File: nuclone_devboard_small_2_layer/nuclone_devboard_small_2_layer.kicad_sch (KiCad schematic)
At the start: 36 parts, among them J1 JTAG_2X05, J2 TYPE-C-31-M-12, J3 nuclone_small_left, J4 nuclone_small_right, SW1 RESET, SW2 Bootloader, U1 MCP1702-MB, U2 TPESD0504C6

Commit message: WIP redoing the template
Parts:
- removed C9: 100n, SquantorRcl:C_0805, symbol Device:C
- C1, C17, C2: footprint SquantorRcl:C_0603 -> SquantorCapacitor:C_0603
- C14, C4: footprint SquantorRcl:C_0402 -> SquantorCapacitor:C_0603
- F1: footprint SquantorRcl:F_0603_hand -> SquantorFuse:F_0603_hand
- FB1: footprint SquantorRcl:L_0603 -> SquantorInductor:L_0603
- H1, H2, H3, H4: footprint MountingHole:MountingHole_3.2mm_M3_Pad_Via -> SquantorPcbOutline:MountingHole_3.2mm_M3_Pad_Via
- R1, R13, R14, R2, R3, R4, R5, R6, R7, R8: footprint SquantorRcl:R_0402_hand -> SquantorResistor:R_0603_hand
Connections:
- net VSS: now also J2.S (Shield)

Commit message: WIP rerouting board and making it common with the medium board
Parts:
- added C5: 100n, SquantorCapacitor:C_0603, symbol Device:C
- added C6: 10u, SquantorCapacitor:C_0603, symbol Device:C
- added R9: 470, SquantorResistor:R_0603_hand, symbol Device:R
- R13: value 100 -> 470
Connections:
- net VBUS: now also C4.1, U2.5 (VDD), C6.1
- net VSS: now also C5.2, C6.2
- net VUSB: no longer C4.1, U2.5 (VDD)
- net Bootloader: no longer names the net of SW2.2
- net Bootloader: now also R9.2; no longer R8.1
- new net BOOT: C5.1, R8.1, R9.1
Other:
- moved on the sheet: C1

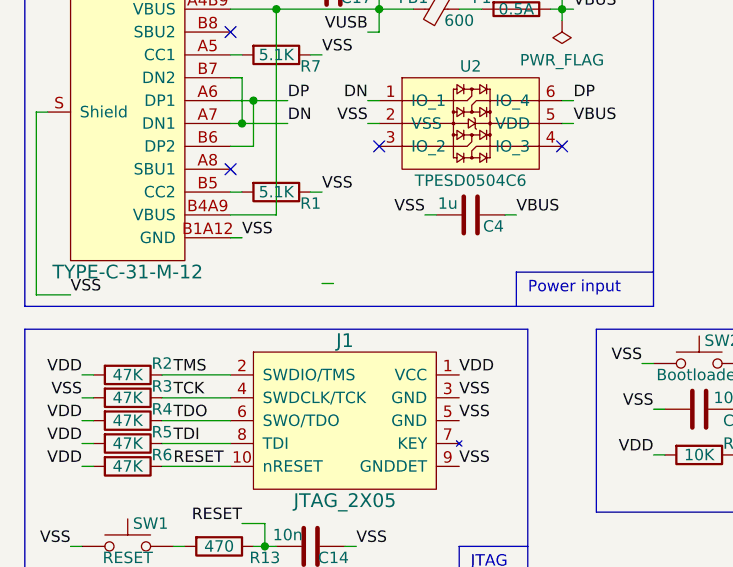
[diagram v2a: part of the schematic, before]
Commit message: P&R done, WIP placing silk items
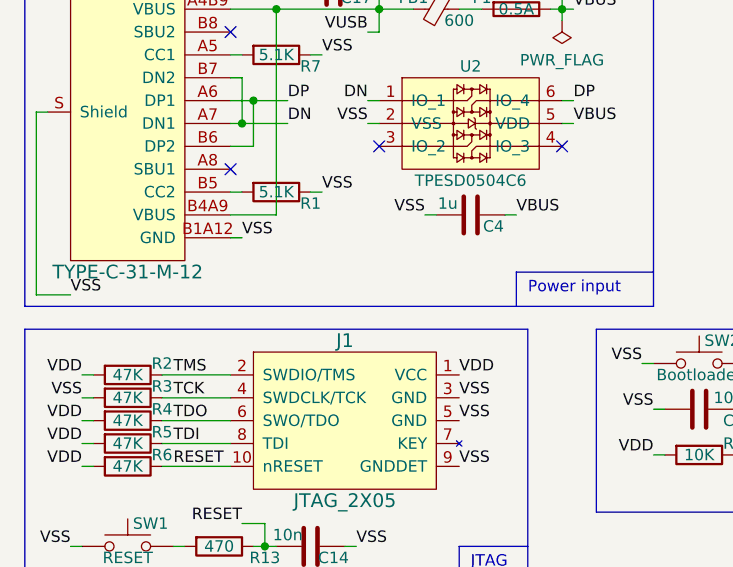
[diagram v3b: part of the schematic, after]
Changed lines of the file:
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@@
-    (stroke (width 0) (type default))
-  )
-  (wire (pts (xy 49.53 118.11) (xy 48.26 118.11))
     (stroke (width 0) (type default))
   )

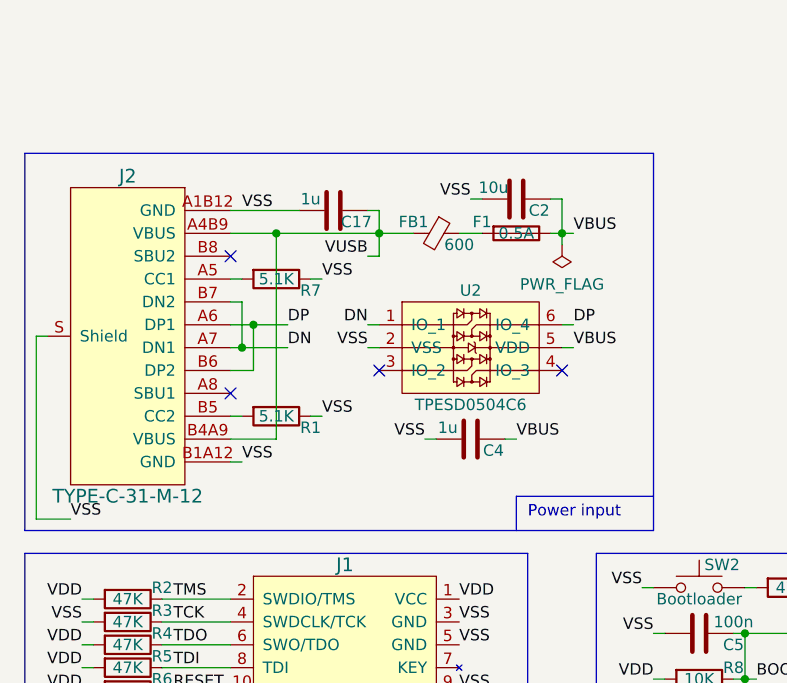
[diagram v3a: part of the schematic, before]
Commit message: added diode to VUSB
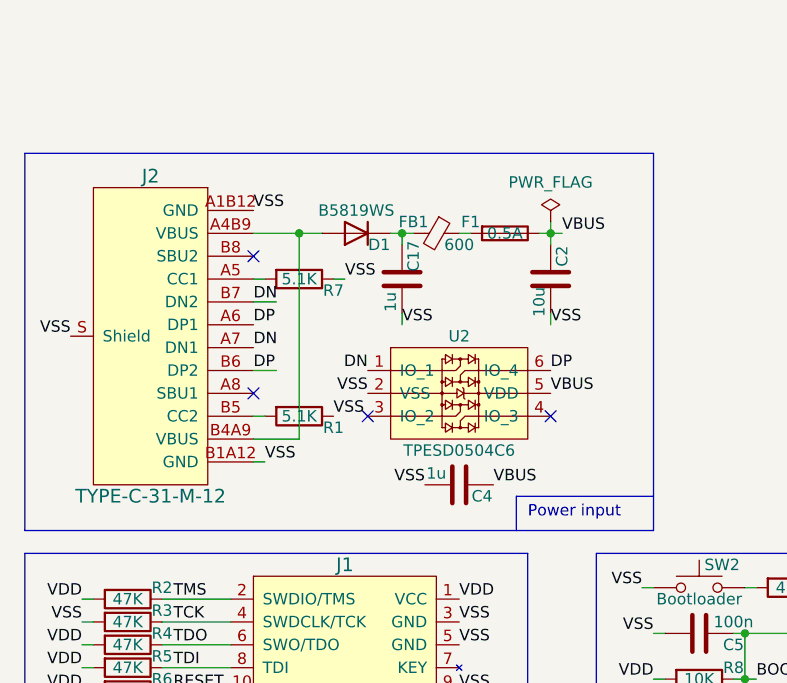
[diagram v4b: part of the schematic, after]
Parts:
- added D1: B5819WS, SquantorDiodes:SOD-323-nexperia-hand, symbol Device:D
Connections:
- net VUSB: no longer names the net of C17.2, FB1.2
- net VUSB: now also D1.1 (K); no longer J2.A4B9 (VBUS), J2.B4A9 (VBUS)
- new net: D1.2 (A), J2.A4B9 (VBUS), J2.B4A9 (VBUS)
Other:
- moved on the sheet: C17, C2, C4, F1, J2, R1, R7, U2
